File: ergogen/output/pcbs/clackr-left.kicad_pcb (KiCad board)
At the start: 2 copper layers, 140.7 x 125.3 mm, 99 parts

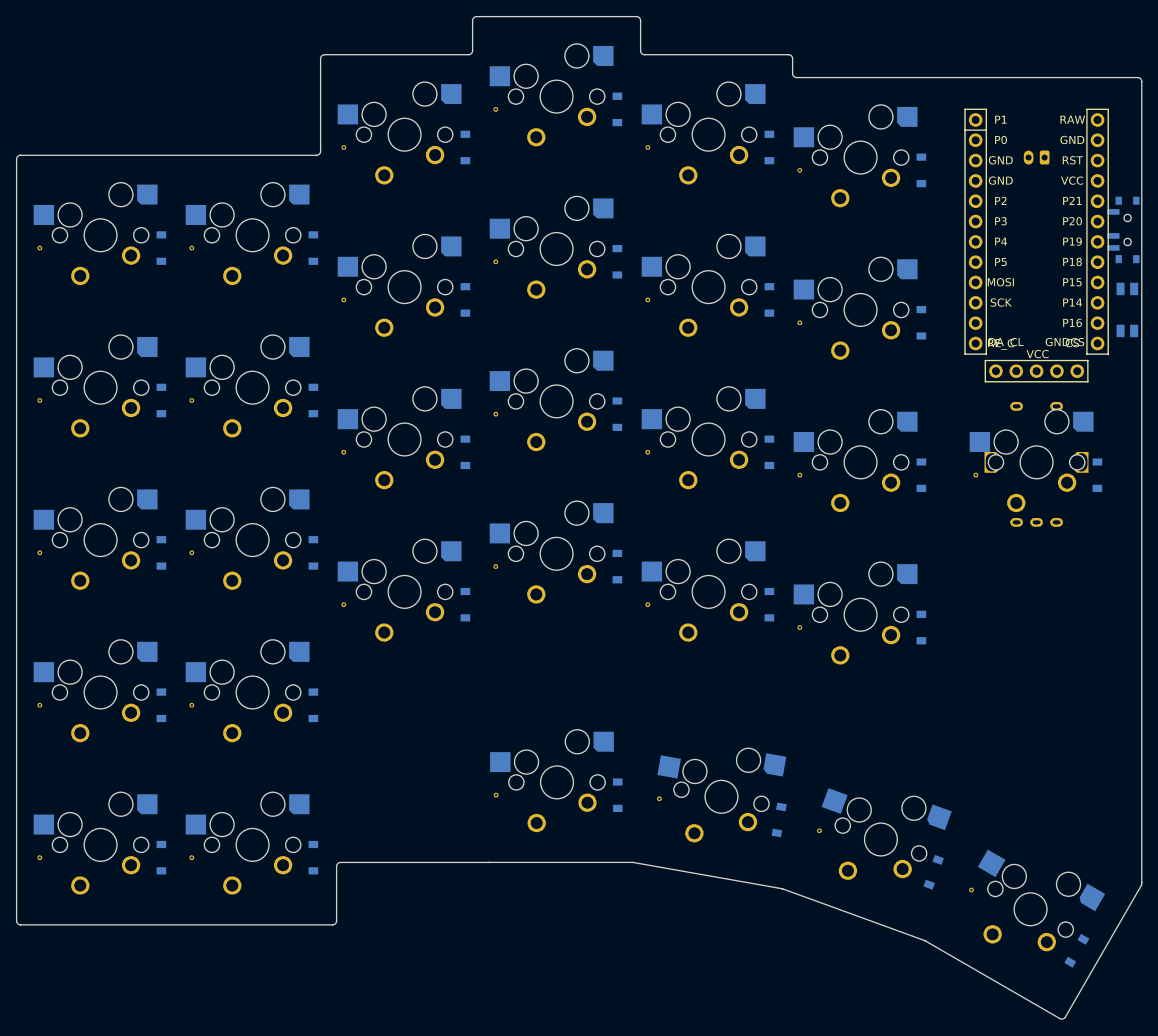
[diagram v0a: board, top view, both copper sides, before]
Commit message: update all outlines
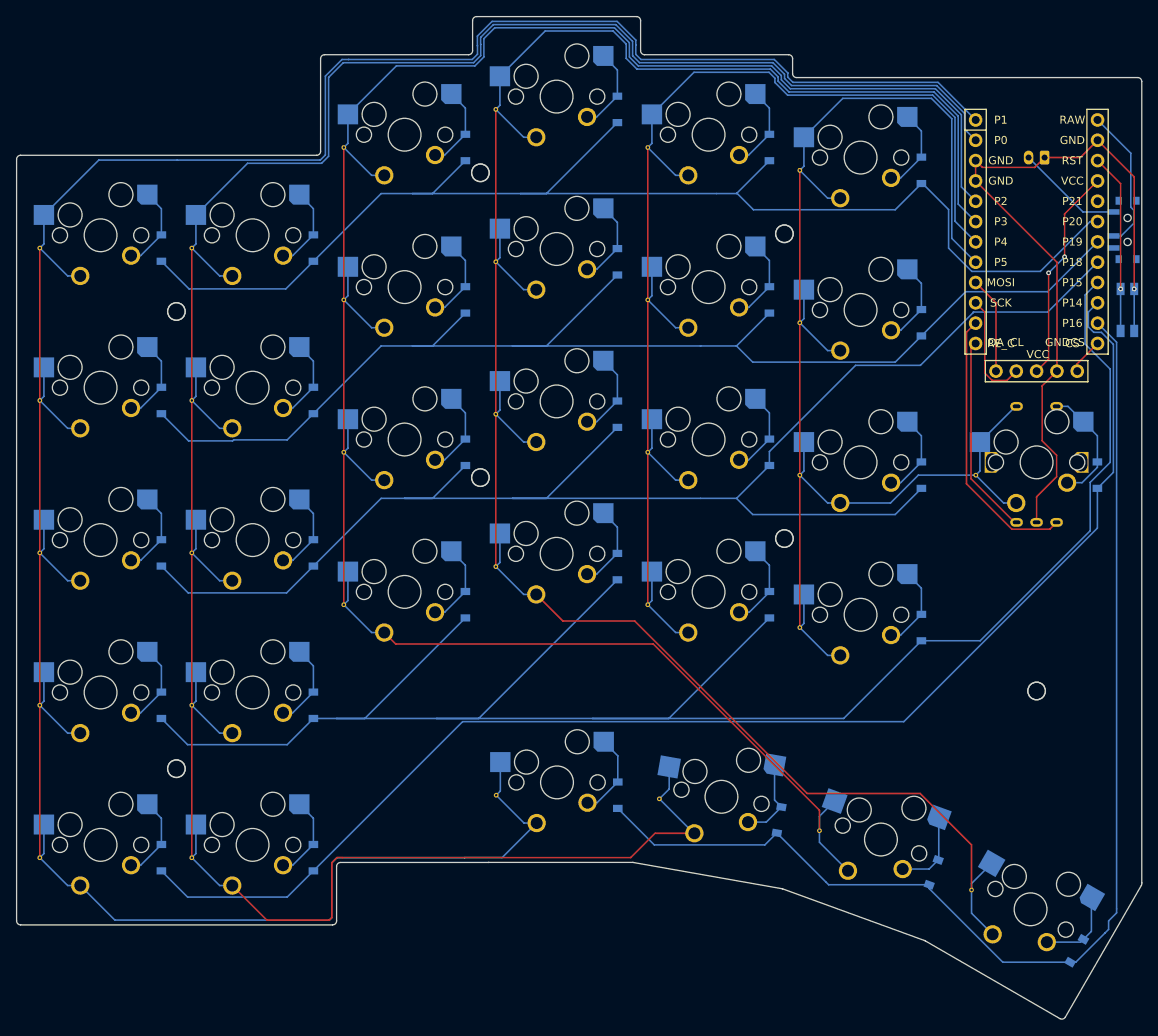
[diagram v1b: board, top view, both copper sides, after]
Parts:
- removed the REF** at (11.4, -74.6)
- removed the REF** at (49.4, -72.9)
- removed the REF** at (49.4, -6.21)
- removed the REF** at (69.8, -5.76)
- removed the REF** at (89.9, -1.77)
- removed the REF** at (108.9, 5.64)
- removed the REF** at (-7.60, -55.6)
- removed the REF** at (-7.60, -74.6)
- removed the REF** at (11.4, -55.6)
- added MH1: , ceoloide:mounting_hole_npth, F.Cu at (9.47, -9.53)
- added MH2: , ceoloide:mounting_hole_npth, F.Cu at (9.47, -66.7)
- added MH3: , ceoloide:mounting_hole_npth, F.Cu at (47.5, -45.9)
- added MH4: , ceoloide:mounting_hole_npth, F.Cu at (47.5, -84.0)
- added MH5: , ceoloide:mounting_hole_npth, F.Cu at (85.5, -38.3)
- added MH6: , ceoloide:mounting_hole_npth, F.Cu at (85.5, -76.4)
- added MH7: , ceoloide:mounting_hole_npth, F.Cu at (117.0, -19.2)
- added REF**: VIA-0.6mm, VIA-0.6mm, F.Cu at (89.9, -1.77)
- added REF**: VIA-0.6mm, VIA-0.6mm, F.Cu at (11.4, -55.5)
- added REF**: VIA-0.6mm, VIA-0.6mm, F.Cu at (11.4, -74.6)
- added REF**: VIA-0.6mm, VIA-0.6mm, F.Cu at (-7.60, -74.6)
- added REF**: VIA-0.6mm, VIA-0.6mm, F.Cu at (69.8, -5.76)
- added REF**: VIA-0.6mm, VIA-0.6mm, F.Cu at (108.9, 5.64)
- added REF**: VIA-0.6mm, VIA-0.6mm, F.Cu at (49.5, -6.21)
- added REF**: VIA-0.6mm, VIA-0.6mm, F.Cu at (-7.60, -55.5)
- added REF**: VIA-0.6mm, VIA-0.6mm, F.Cu at (49.4, -72.9)
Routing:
- net P1: track 0.00 -> 349.3 mm
- net P0: track 0.00 -> 332.2 mm
- net P2: track 0.00 -> 277.6 mm
- net P3: track 0.00 -> 264.1 mm
- net P15: track 0.00 -> 240.9 mm
- net P18: track 0.00 -> 187.9 mm
- net P5: track 0.00 -> 177.0 mm
- net P14: track 0.00 -> 168.8 mm
- net P20: track 0.00 -> 165.4 mm
- net P19: track 0.00 -> 161.3 mm
- net P4: track 0.00 -> 159.9 mm
- net P16: track 0.00 -> 149.7 mm
- net GND: track 0.00 -> 94.7 mm, vias 0 -> 1
- net RE_A: track 0.00 -> 34.5 mm
- net VCC: track 0.00 -> 26.9 mm, vias 0 -> 2
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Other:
- outline, holes or cut-outs redrawn
